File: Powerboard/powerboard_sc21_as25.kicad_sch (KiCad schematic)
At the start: 53 parts, among them J2 Conn_01x02_Male, J3 Conn_01x02_Male, J4 Conn_01x08_Male, Q6 MMDT2222A, Q7 RSJ250P10TL, Q8 RSJ250P10TL, U1 LTC4412xS6, U2 SN65HVD230, U3 ESP32-PICO-D4

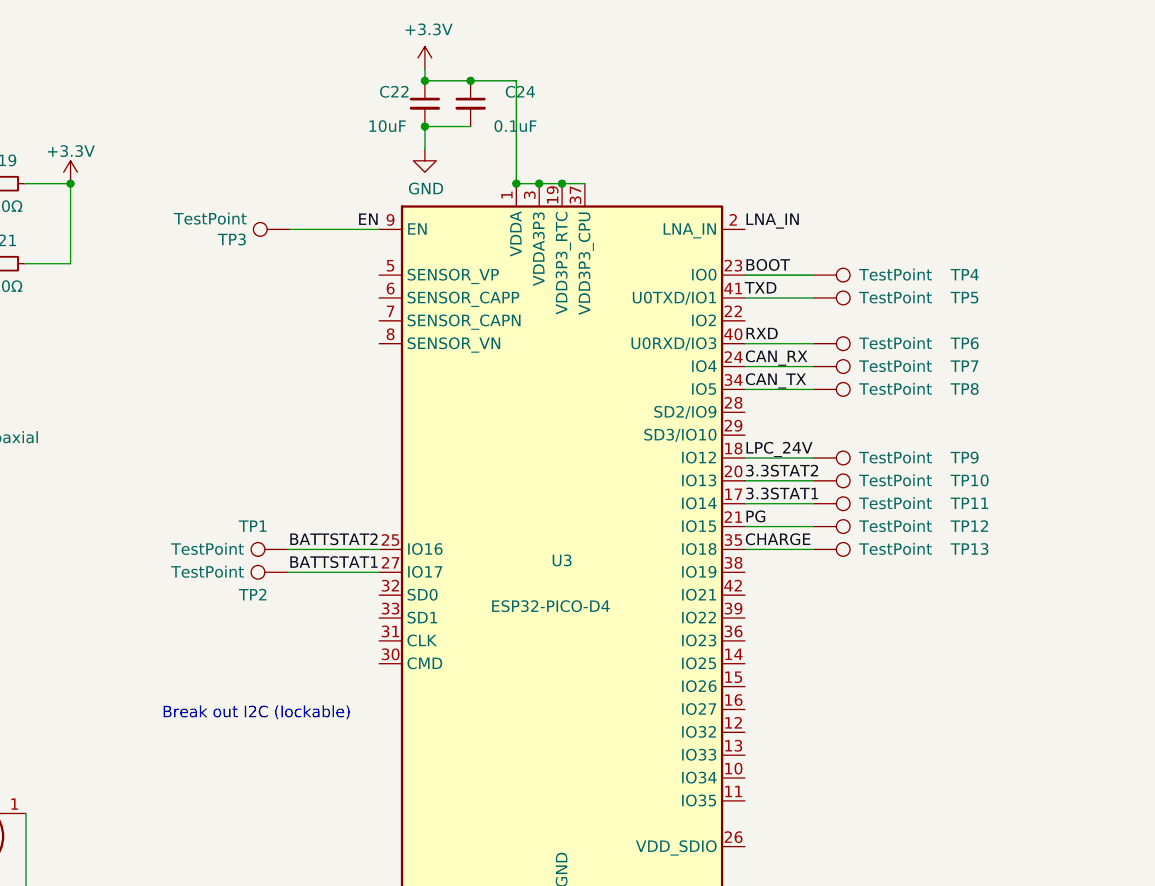
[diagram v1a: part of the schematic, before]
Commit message: changed old mosfets, broke out I2C
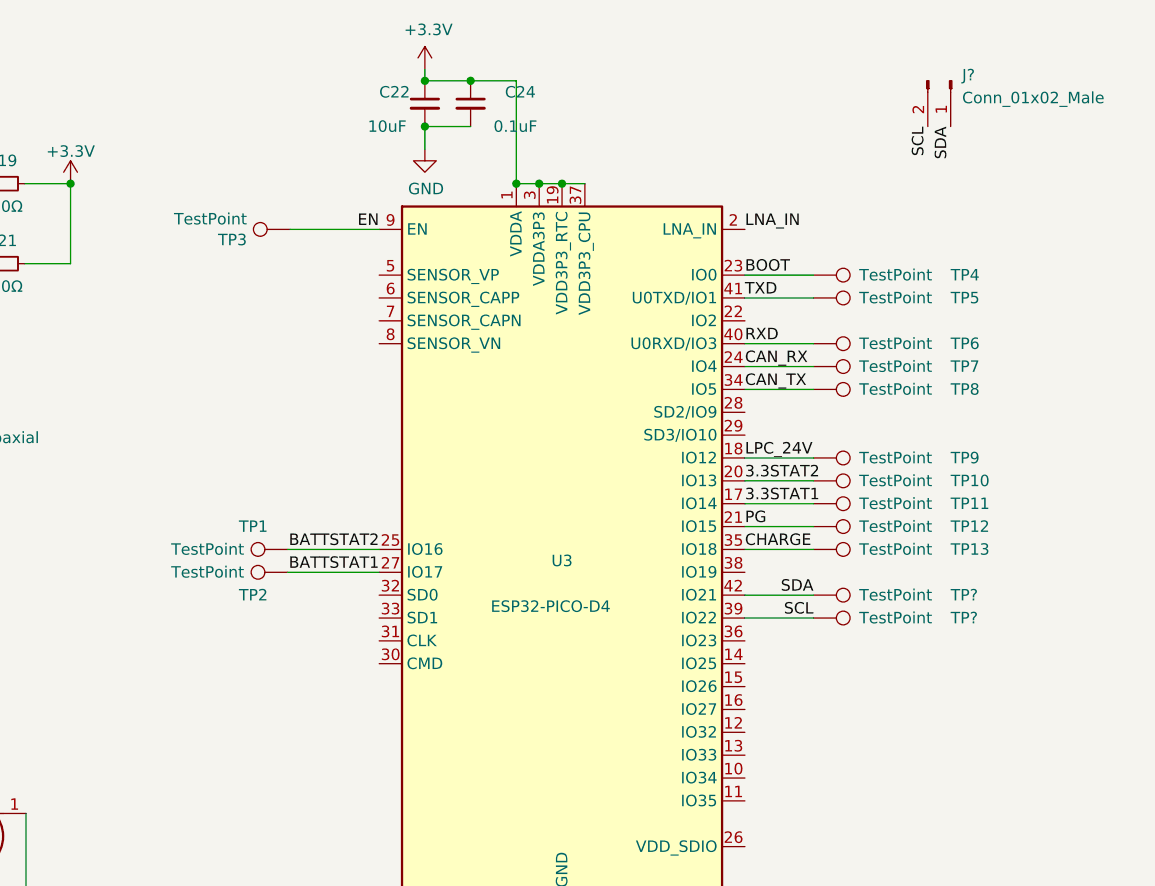
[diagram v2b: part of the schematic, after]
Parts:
- added J?: Conn_01x02_Male, symbol Connector:Conn_01x02_Male
- added TP? (x2): TestPoint, symbol Connector:TestPoint
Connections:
- net SCL: now reaches U3.39 (IO22)
- net SCL: now also J?.2 (Pin_2), TP?.1
- net SDA: now reaches U3.42 (IO21)
- net SDA: now also J?.1 (Pin_1), TP?.1
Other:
- note removed: "Break out I2C (lockable)"
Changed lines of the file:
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@@
+    (stroke (width 0) (type default) (color 0 0 0 0))
+  )
+  (wire (pts (xy 237.49 78.74) (xy 245.11 78.74))
     (stroke (width 0) (type default) (color 0 0 0 0))
   )
@@
     (stroke (width 0) (type default) (color 0 0 0 0))
   )
+  (wire (pts (xy 237.49 81.28) (xy 245.11 81.28))
+    (stroke (width 0) (type default) (color 0 0 0 0))
+  )
   (wire (pts (xy 237.49 73.66) (xy 245.11 73.66))
     (stroke (width 0) (type default) (color 0 0 0 0))
@@
   (wire (pts (xy 109.22 46.99) (xy 109.22 49.53))
     (stroke (width 0) (type default) (color 0 0 0 0))
-  )
-  (text "Break out I2C (lockable)\n" (at 172.72 92.71 0)
-    (effects (font (size 1.27 1.27)) (justify left bottom))
   )
   (label "CANH" (at 136.398 171.196 0)
@@
     (effects (font (size 1.27 1.27)) (justify right bottom))
   )
+  (label "SCL" (at 245.11 81.28 180)
+    (effects (font (size 1.27 1.27)) (justify right bottom))
+  )
   (label "CAN_TX" (at 237.49 55.88 0)
     (effects (font (size 1.27 1.27)) (justify left bottom))
@@
     (effects (font (size 1.27 1.27)) (justify left bottom))
   )
+  (label "SDA" (at 260.35 26.67 270)
+    (effects (font (size 1.27 1.27)) (justify right bottom))
+  )
   (label "EN" (at 93.98 27.94 180)
     (effects (font (size 1.27 1.27)) (justify right bottom))
@@
     (effects (font (size 1.27 1.27)) (justify left bottom))
   )
+  (label "SCL" (at 257.81 26.67 270)
+    (effects (font (size 1.27 1.27)) (justify right bottom))
+  )
   (label "EN" (at 62.23 26.67 0)
     (effects (font (size 1.27 1.27)) (justify left bottom))
@@
   (label "Vref" (at 226.06 146.05 0)
     (effects (font (size 1.27 1.27)) (justify left bottom))
+  )
+  (label "SDA" (at 245.11 78.74 180)
+    (effects (font (size 1.27 1.27)) (justify right bottom))
   )
   (label "LPC_24V" (at 237.49 63.5 0)
@@
     (pin "3")
   )
+  (symbol (lib_id "Connector:Conn_01x02_Male") (at 260.35 21.59 270) (unit 1)
+    (in_bom yes) (on_board yes) (fields_autoplaced)
+    (property "Reference" "J?" (id 0) (at 261.62 20.9549 90)
+      (effects (font (size 1.27 1.27)) (justify left))
+    )
+    (property "Value" "Conn_01x02_Male" (id 1) (at 261.62 23.4949 90)
+      (effects (font (size 1.27 1.27)) (justify left))
+    )
+    (property "Footprint" "" (id 2) (at 260.35 21.59 0)
+      (effects (font (size 1.27 1.27)) hide)
+    )
+    (property "Datasheet" "~" (id 3) (at 260.35 21.59 0)
+      (effects (font (size 1.27 1.27)) hide)
+    )
+    (pin "1")
+    (pin "2")
+  )
   (symbol (lib_id "Connector:TestPoint") (at 186.944 38.1 90) (unit 1)
     (in_bom yes) (on_board yes)
@@
     (pin "2")
   )
+  (symbol (lib_id "Connector:TestPoint") (at 245.11 78.74 270) (unit 1)
+    (in_bom yes) (on_board yes)
+    (property "Reference" "TP?" (id 0) (at 260.35 78.74 90)
+      (effects (font (size 1.27 1.27)) (justify left))
+    )
+    (property "Value" "TestPoint" (id 1) (at 250.19 78.74 90)
+      (effects (font (size 1.27 1.27)) (justify left))
+    )
+    (property "Footprint" "" (id 2) (at 245.11 83.82 0)
+      (effects (font (size 1.27 1.27)) hide)
+    )
+    (property "Datasheet" "~" (id 3) (at 245.11 83.82 0)
+      (effects (font (size 1.27 1.27)) hide)
+    )
+    (pin "1")
+  )
+  (symbol (lib_id "Connector:TestPoint") (at 245.11 81.28 270) (unit 1)
+    (in_bom yes) (on_board yes)
+    (property "Reference" "TP?" (id 0) (at 260.35 81.28 90)
+      (effects (font (size 1.27 1.27)) (justify left))
+    )
+    (property "Value" "TestPoint" (id 1) (at 250.19 81.28 90)
+      (effects (font (size 1.27 1.27)) (justify left))
+    )
+    (property "Footprint" "" (id 2) (at 245.11 86.36 0)
+      (effects (font (size 1.27 1.27)) hide)
+    )
+    (property "Datasheet" "~" (id 3) (at 245.11 86.36 0)
+      (effects (font (size 1.27 1.27)) hide)
+    )
+    (pin "1")
+  )
   (symbol (lib_id "Device:LED") (at 148.59 41.91 0) (unit 1)
     (in_bom yes) (on_board yes)
@@
       (reference "#PWR0171") (unit 1) (value "GND") (footprint "")
     )
-    (path "/b1853ee1-af2e-49ab-93e4-e29b2d9f793d/ba910aa5-1c14-49e2-8e02-8063979f6496"
-      (reference "#PWR0172") (unit 1) (value "GND") (footprint "")
-    )
-    (path "/b1853ee1-af2e-49ab-93e4-e29b2d9f793d/a4e693f1-e8be-4638-b20a-f43f39a9ed46"
-      (reference "#PWR0173") (unit 1) (value "GND") (footprint "")
-    )
     (path "/b1853ee1-af2e-49ab-93e4-e29b2d9f793d/b36e399c-fd07-48dc-9ff5-2204b47fbf43"
       (reference "#PWR0174") (unit 1) (value "GND") (footprint "")
@@
       (reference "C54") (unit 1) (value "10uF") (footprint "Capacitor_SMD:C_0603_1608Metric")
     )
-    (path "/b1853ee1-af2e-49ab-93e4-e29b2d9f793d/3bf9d9e3-3041-4ea1-ad6f-34bc1dc2c61a"
-      (reference "C55") (unit 1) (value "1uF") (footprint "Capacitor_SMD:C_0603_1608Metric")
-    )
-    (path "/b1853ee1-af2e-49ab-93e4-e29b2d9f793d/1fd2c422-69ae-40c0-b3b2-cb505077339f"
-      (reference "C56") (unit 1) (value "0.1uF") (footprint "Capacitor_SMD:C_0603_1608Metric")
-    )
     (path "/b1853ee1-af2e-49ab-93e4-e29b2d9f793d/900cbe97-baf8-4c02-a824-562c02dac994"
       (reference "C57") (unit 1) (value "10uF") (footprint "Capacitor_SMD:C_0603_1608Metric")
@@
       (reference "J?") (unit 1) (value "Conn_Coaxial") (footprint "Connector_Coaxial:U.FL_Molex_MCRF_73412-0110_Vertical")
     )
+    (path "/515e8bdb-6536-45a5-ad34-da4f3e68b654"
+      (reference "J?") (unit 1) (value "Conn_01x02_Male") (footprint "")
+    )
     (path "/a9c6c562-c597-48be-b814-c3219c333b03"
       (reference "JP?") (unit 1) (value "SolderJumper_2_Open") (footprint "")
@@
       (reference "PowerLED1") (unit 1) (value "LED") (footprint "")
     )
-    (path "/00000000-0000-0000-0000-000061beb629/00000000-0000-0000-0000-0000621270b4"
-      (reference "Q1") (unit 1) (value "SI7617DN-T1-GE3") (footprint "SIS862DNT1GE3")
-    )
-    (path "/00000000-0000-0000-0000-000061beb629/00000000-0000-0000-0000-0000621d4ed7"
-      (reference "Q2") (unit 1) (value "SI7617DN-T1-GE3") (footprint "SIS862DNT1GE3")
-    )
-    (path "/00000000-0000-0000-0000-000061beb629/00000000-0000-0000-0000-0000621b9708"
-      (reference "Q3") (unit 1) (value "SI7617DN-T1-GE3") (footprint "SIS862DNT1GE3")
-    )
-    (path "/00000000-0000-0000-0000-000061beb629/00000000-0000-0000-0000-00006217044a"
-      (reference "Q4") (unit 1) (value "SIS412DN-T1-GE3-iclr") (footprint "POWERPAK-1212-8")
-    )
-    (path "/00000000-0000-0000-0000-000061beb629/00000000-0000-0000-0000-00006218830c"
-      (reference "Q5") (unit 1) (value "SIS412DN-T1-GE3-iclr") (footprint "POWERPAK-1212-8")
+    (path "/00000000-0000-0000-0000-000061beb629/1fa6e3d4-ed6a-45aa-b12d-58ffcaf26a3e"
+      (reference "Q1") (unit 1) (value "RSJ250P10TL") (footprint "RSJ151P10TL")
+    )
+    (path "/00000000-0000-0000-0000-000061beb629/bcaaa00c-c7ff-4122-9a9e-b95e6a3661ad"
+      (reference "Q2") (unit 1) (value "RSJ250P10TL") (footprint "RSJ151P10TL")
+    )
+    (path "/00000000-0000-0000-0000-000061beb629/2cda51fe-2b5f-42b4-99f9-7b4945740e04"
+      (reference "Q3") (unit 1) (value "RSJ250P10TL") (footprint "RSJ151P10TL")
+    )
+    (path "/00000000-0000-0000-0000-000061beb629/7603b326-8e82-4c2c-8430-3e8cccc8c7da"
+      (reference "Q4") (unit 1) (value "RS1G120MN") (footprint "Package_SO:HSOP-8-1EP_3.9x4.9mm_P1.27mm_EP2.41x3.1mm")
+    )
+    (path "/00000000-0000-0000-0000-000061beb629/c7dafbd3-82da-4a26-b0f9-de0dc400a5f9"
+      (reference "Q5") (unit 1) (value "RS1G120MN") (footprint "Package_SO:HSOP-8-1EP_3.9x4.9mm_P1.27mm_EP2.41x3.1mm")
     )
     (path "/c0f697a9-8366-44b8-9e73-0bc4f4e97245"
@@
       (reference "Q8") (unit 1) (value "RSJ250P10TL") (footprint "RSJ151P10TL")
     )
-    (path "/00000000-0000-0000-0000-000061f04c1a/00000000-0000-0000-0000-000062124ed0"
-      (reference "Q12") (unit 1) (value "CSD25485F5T-iclr") (footprint "CSD13385F5")
-    )
-    (path "/00000000-0000-0000-0000-000061f04c1a/dfd28551-2c8c-4565-a789-337964cf9538"
-      (reference "Q?") (unit 1) (value "CSD25485F5T-iclr") (footprint "CSD13385F5")
+    (path "/00000000-0000-0000-0000-000061f04c1a/645087d6-6154-4e63-9c47-337ee4493649"
+      (reference "Q?") (unit 1) (value "MCH6351") (footprint "")
+    )
+    (path "/00000000-0000-0000-0000-000061f04c1a/95d2c580-3918-4410-8709-4870c69f970f"
+      (reference "Q?") (unit 1) (value "MCH6351") (footprint "")
     )
     (path "/00000000-0000-0000-0000-000061beb629/00000000-0000-0000-0000-000061c2a900"
@@
       (reference "R40") (unit 1) (value "4.7k") (footprint "")
     )
-    (path "/b1853ee1-af2e-49ab-93e4-e29b2d9f793d/08599c5d-18df-4076-8d95-9afe2b0b7202"
-      (reference "R41") (unit 1) (value "100k") (footprint "Resistor_SMD:R_0603_1608Metric")
-    )
     (path "/b1853ee1-af2e-49ab-93e4-e29b2d9f793d/a6bf9111-8852-4077-bff6-579c92450f65"
-      (reference "R42") (unit 1) (value "147k") (footprint "Resistor_SMD:R_0603_1608Metric")
+      (reference "R42") (unit 1) (value "56k") (footprint "Resistor_SMD:R_0603_1608Metric")
     )
     (path "/b1853ee1-af2e-49ab-93e4-e29b2d9f793d/1f07eb91-ef46-4237-a9f5-5823737e0d44"
-      (reference "R43") (unit 1) (value "47k") (footprint "Resistor_SMD:R_0603_1608Metric")
+      (reference "R43") (unit 1) (value "10k") (footprint "Resistor_SMD:R_0603_1608Metric")
     )
     (path "/00000000-0000-0000-0000-000061beb629/00000000-0000-0000-0000-000061c1bdbb"
@@
       (reference "TP25") (unit 1) (value "TestPoint") (footprint "")
     )
+    (path "/de610fa4-8359-41ae-a8e8-613d78621be4"
+      (reference "TP?") (unit 1) (value "TestPoint") (footprint "")
+    )
+    (path "/dea2ce42-f49f-4b86-a5e4-fccc85d3b555"
+      (reference "TP?") (unit 1) (value "TestPoint") (footprint "")
+    )
     (path "/00000000-0000-0000-0000-00006211988f"

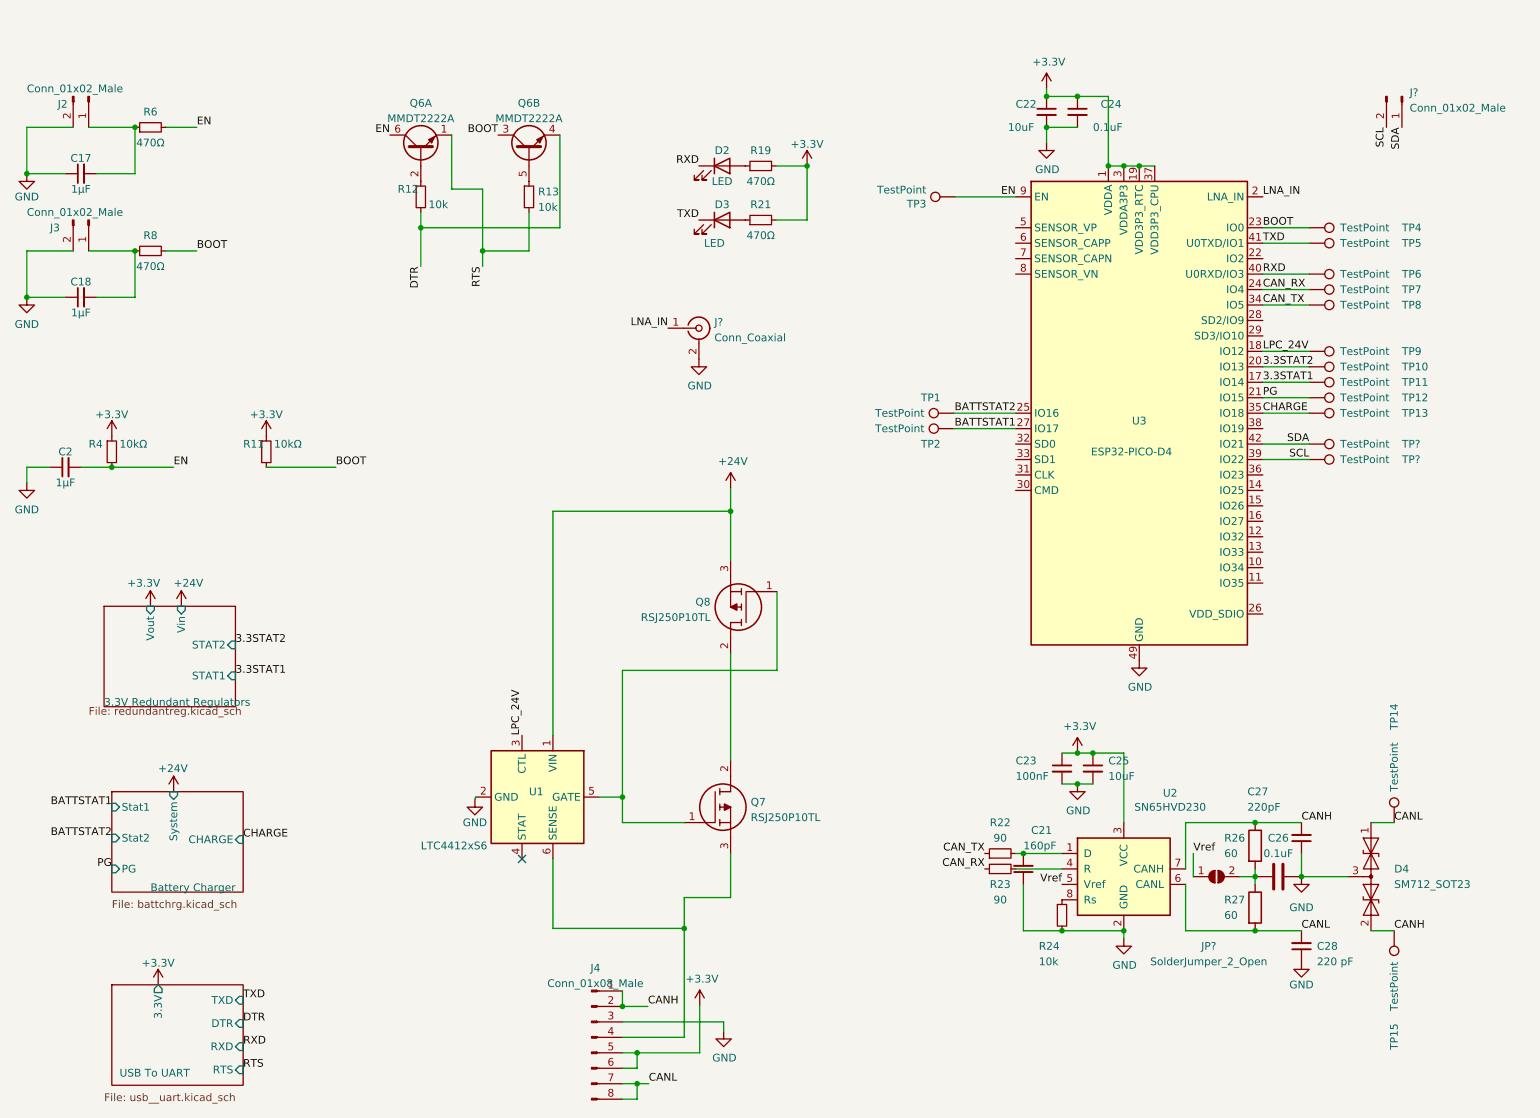
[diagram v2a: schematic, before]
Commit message: 3v3 reg cap & inductor changes, added boost capacitor
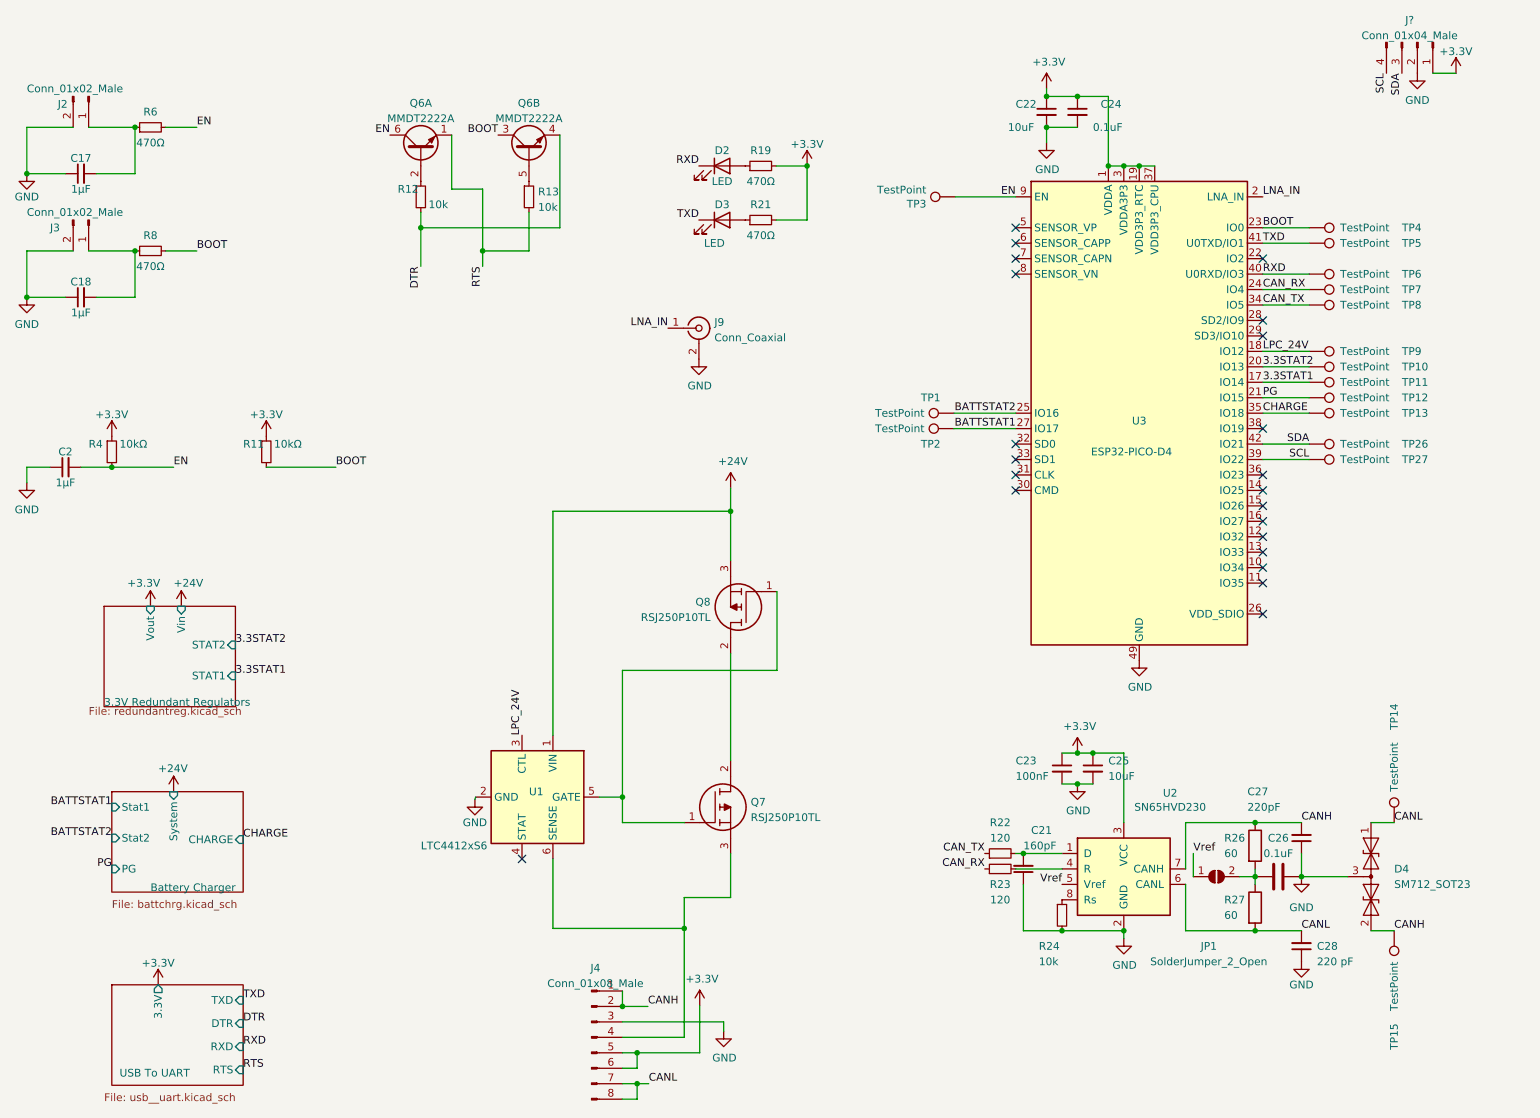
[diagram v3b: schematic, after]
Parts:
- removed J?: Conn_01x02_Male, symbol Connector:Conn_01x02_Male
- added J?: Conn_01x04_Male, symbol Connector:Conn_01x04_Male
- D2, D3: footprint (none) -> LED_SMD:LED_0603_1608Metric
- J2, J3: footprint (none) -> Connector_PinHeader_2.54mm:PinHeader_1x02_P2.54mm_Vertical
- JP1: renamed from JP?; footprint (none) -> Jumper:SolderJumper-3_P1.3mm_Open_RoundedPad1.0x1.5mm
- R22, R23: value 90 -> 120
- TP1, TP10, TP11, TP12, TP13, TP14, TP15, TP2, TP3, TP4, TP5, TP6, TP7, TP8, TP9: footprint (none) -> TestPoint:TestPoint_Pad_D1.0mm
- TP26, TP27: renamed from TP?; footprint (none) -> TestPoint:TestPoint_Pad_D1.0mm
- gave numbers to parts that had none: 1
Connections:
- net +3V3: now also J?.1 (Pin_1)
- net GND: now also J?.2 (Pin_2)
- net SCL: now also J?.4 (Pin_4)
- net SDA: now also J?.3 (Pin_3)
- no-connect marks 1 -> 22
